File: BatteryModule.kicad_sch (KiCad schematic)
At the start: 38 parts, among them J1 USB, J2 OUT, J3 USB_C_Receptacle_PowerOnly_6P, J4 BAT, U1 TLV76701DRVx, U2 TP4056-42-ESOP8, U3 TLV61048DBVR

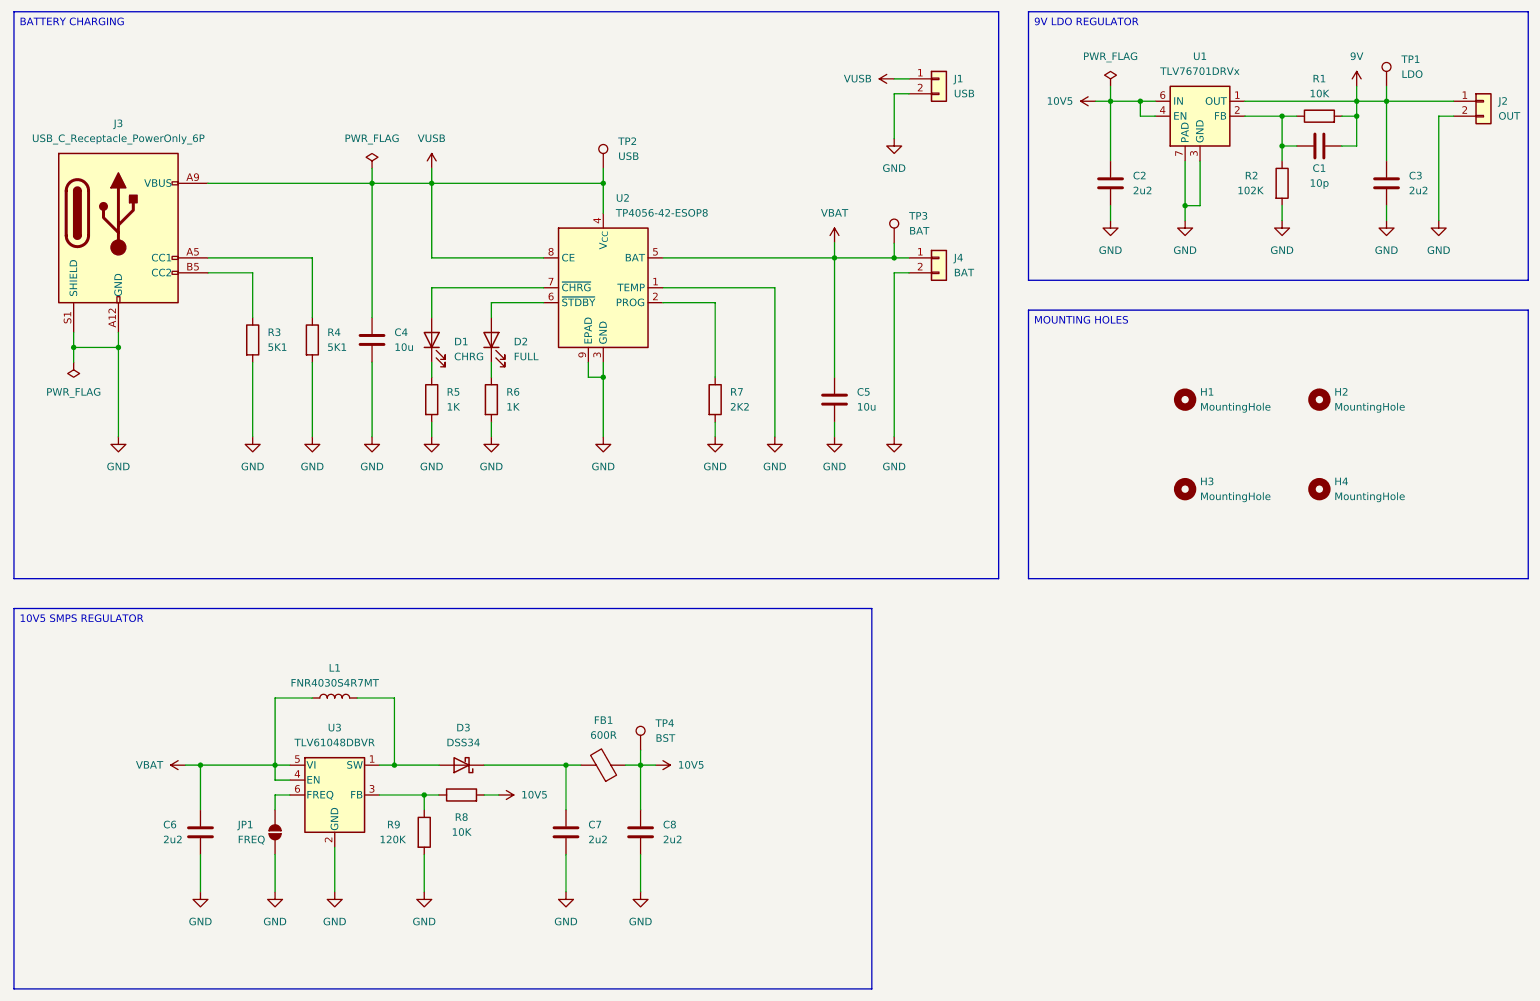
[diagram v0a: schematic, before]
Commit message: Modified design structure
Added a battery sheet for the schematic.
Added a regulator sheet for the schematic.
Updated board layout.
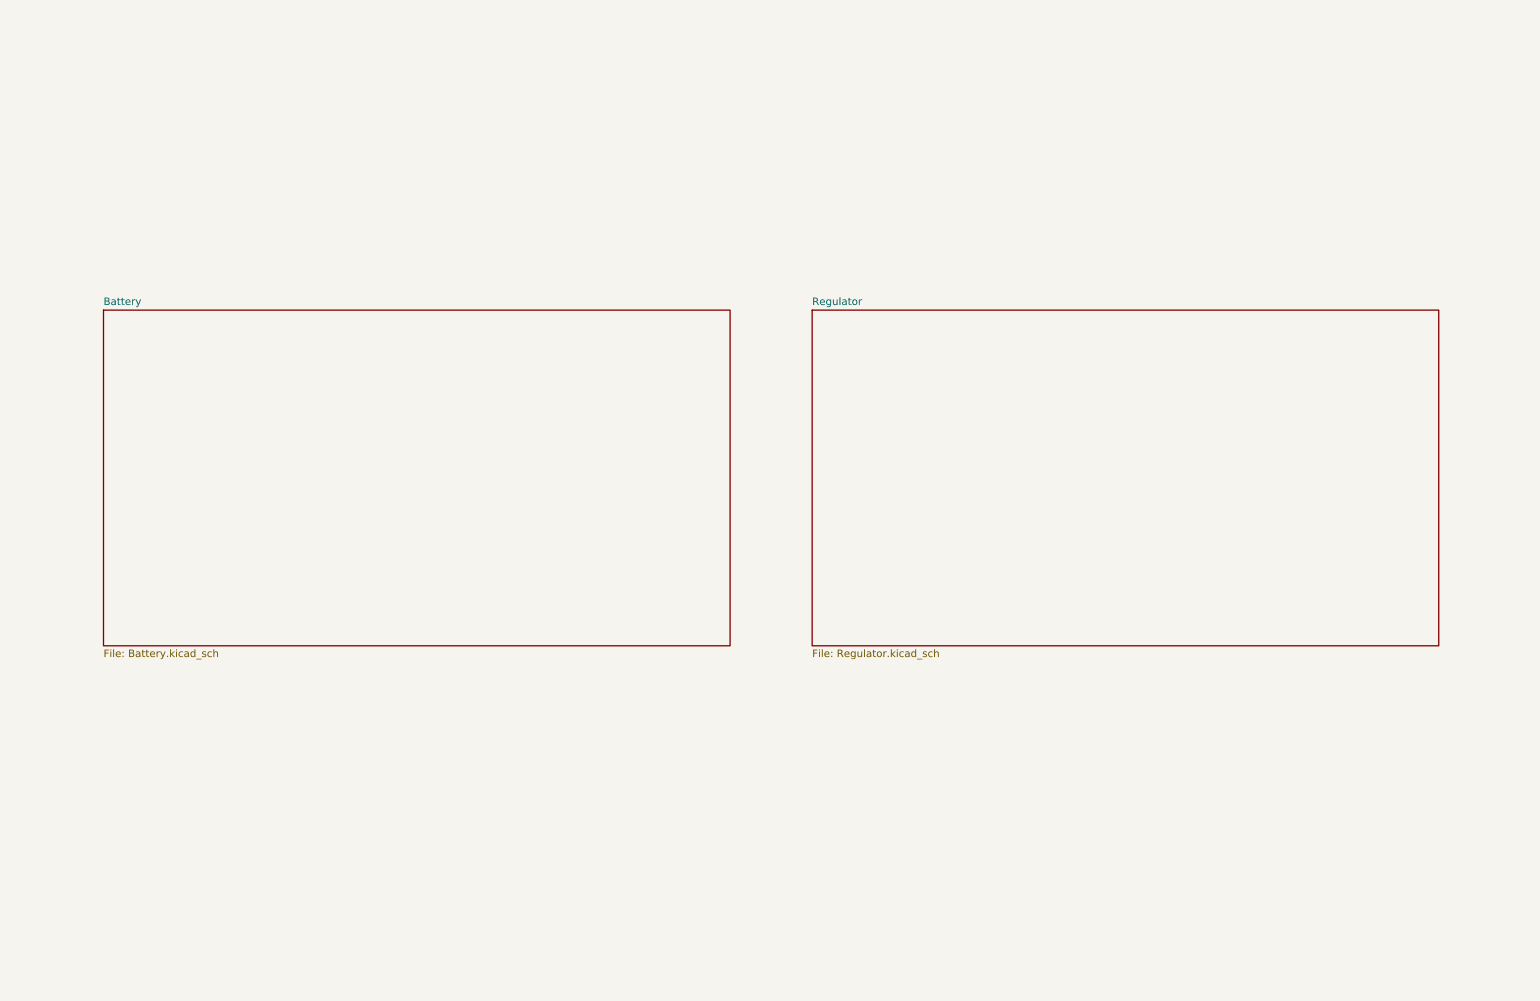
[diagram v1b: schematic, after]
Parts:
- removed C1: 10p, Capacitor_SMD:C_0805_2012Metric_Pad1.18x1.45mm_HandSolder, symbol Device:C
- removed C2, C3, C6, C7, C8: 2u2, Capacitor_SMD:C_1206_3216Metric_Pad1.33x1.80mm_HandSolder, symbol Device:C
- removed C4, C5: 10u, Capacitor_SMD:C_1206_3216Metric_Pad1.33x1.80mm_HandSolder, symbol Device:C
- removed D1: CHRG, LED_SMD:LED_0805_2012Metric_Pad1.15x1.40mm_HandSolder, symbol Device:LED
- removed D2: FULL, LED_SMD:LED_0805_2012Metric_Pad1.15x1.40mm_HandSolder, symbol Device:LED
- removed D3: DSS34, Diode_SMD:D_SOD-123F, symbol Device:D_Schottky
- removed FB1: 600R, Inductor_SMD:L_0805_2012Metric, symbol Device:FerriteBead
- removed H1, H2, H3, H4: MountingHole, MountingHole:MountingHole_3.2mm_M3, symbol Mechanical:MountingHole
- removed J1: USB, Custom_Parts:JST_PH_1x02_P2.00MM_VERT, symbol Connector_Generic:Conn_01x02
- removed J2: OUT, Custom_Parts:JST_PH_1x02_P2.00MM_VERT, symbol Connector_Generic:Conn_01x02
- removed J3: USB_C_Receptacle_PowerOnly_6P, Connector_USB:USB_C_Receptacle_GCT_USB4125-xx-x_6P_TopMnt_Horizontal, symbol Connector:USB_C_Receptacle_PowerOnly_6P
- removed J4: BAT, Custom_Parts:JST_PH_1x02_P2.00MM_VERT, symbol Connector_Generic:Conn_01x02
- removed JP1: FREQ, Jumper:SolderJumper-2_P1.3mm_Open_RoundedPad1.0x1.5mm, symbol Jumper:SolderJumper_2_Open
- removed L1: FNR4030S4R7MT, Inductor_SMD:L_Changjiang_FNR4030S, symbol Device:L
- removed R1, R8: 10K, Resistor_SMD:R_0805_2012Metric_Pad1.20x1.40mm_HandSolder, symbol Device:R
- removed R2: 102K, Resistor_SMD:R_0805_2012Metric_Pad1.20x1.40mm_HandSolder, symbol Device:R
- removed R3, R4: 5K1, Resistor_SMD:R_0805_2012Metric_Pad1.20x1.40mm_HandSolder, symbol Device:R
- removed R5, R6: 1K, Resistor_SMD:R_0805_2012Metric_Pad1.20x1.40mm_HandSolder, symbol Device:R
- removed R7: 2K2, Resistor_SMD:R_0805_2012Metric_Pad1.20x1.40mm_HandSolder, symbol Device:R
- removed R9: 120K, Resistor_SMD:R_0805_2012Metric_Pad1.20x1.40mm_HandSolder, symbol Device:R
- removed TP1: LDO, TestPoint:TestPoint_Pad_D1.0mm, symbol Connector:TestPoint
- removed TP2: USB, TestPoint:TestPoint_Pad_D1.0mm, symbol Connector:TestPoint
- removed TP3: BAT, TestPoint:TestPoint_Pad_D1.0mm, symbol Connector:TestPoint
- removed TP4: BST, TestPoint:TestPoint_Pad_D1.0mm, symbol Connector:TestPoint
- removed U1: TLV76701DRVx, Package_SON:WSON-6-1EP_2x2mm_P0.65mm_EP1x1.6mm_ThermalVias, symbol Regulator_Linear:TLV76701DRVx
- removed U2: TP4056-42-ESOP8, Custom_Parts:SOIC-8-1EP_3.9x4.9MM_P1.27MM_EP2.41x3.3MM, symbol Battery_Management:TP4056-42-ESOP8
- removed U3: TLV61048DBVR, Package_TO_SOT_SMD:SOT-23-6, symbol Custom_Parts:TLV61048DBVR
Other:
- added sheet Battery (Battery.kicad_sch)
- added sheet Regulator (Regulator.kicad_sch)
